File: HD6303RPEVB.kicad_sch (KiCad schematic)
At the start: 36 parts, among them J16 Conn_01x08, J2 Conn_01x06, SW1 Reset, U1 74HC00, U2 HD6303RP, U3 CY62256-70PC, U4 CY62256-70PC, U5 28C64, U6 74HC373, U7 74HC373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

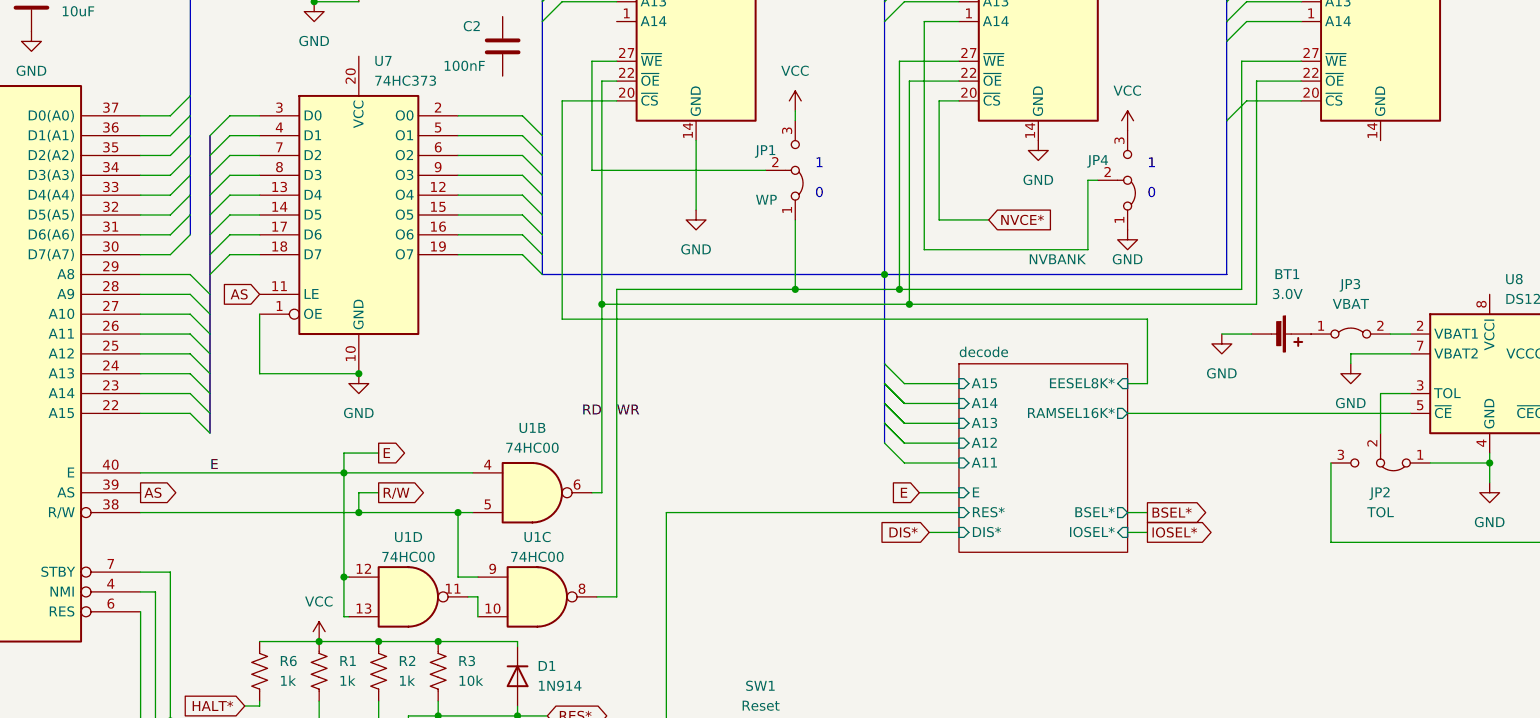
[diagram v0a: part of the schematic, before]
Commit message: Fixed bug in RD/WR circuitry.
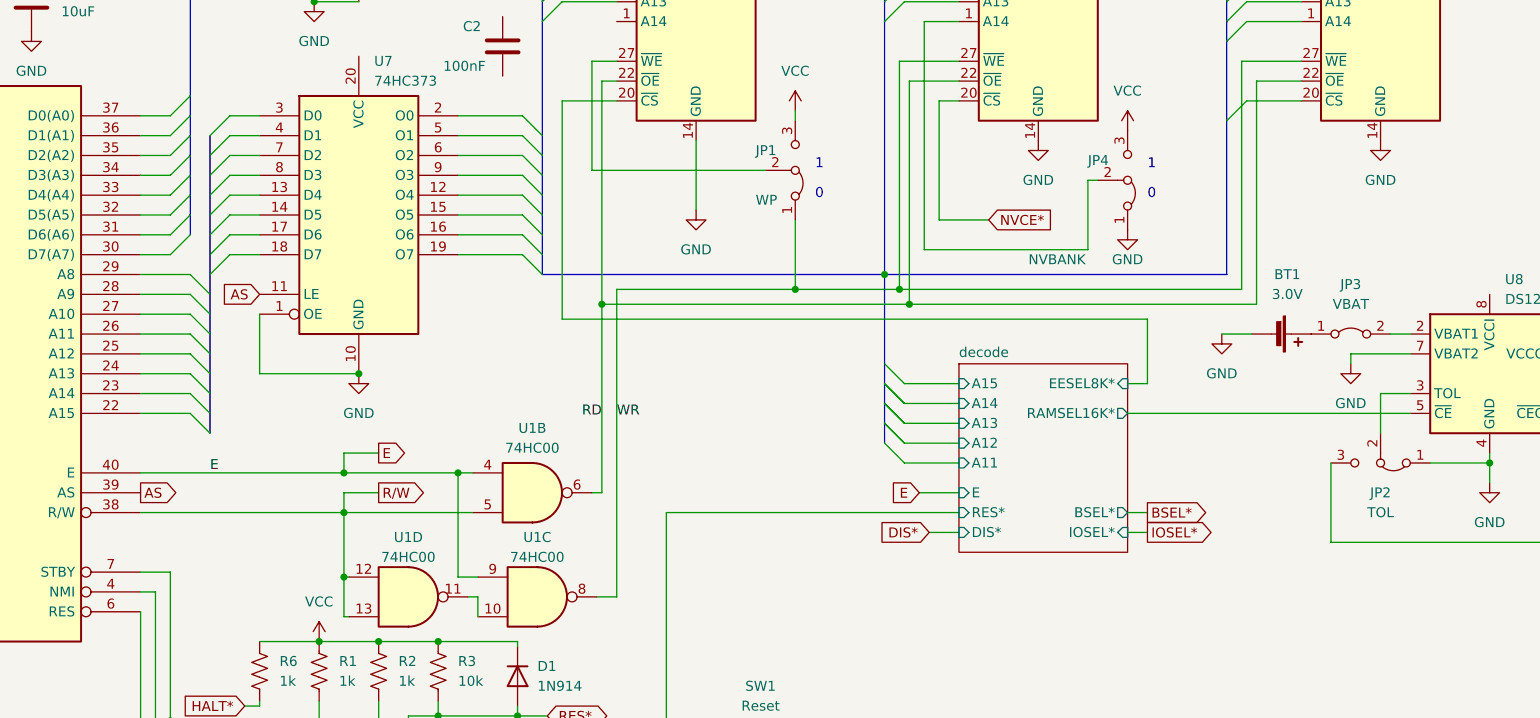
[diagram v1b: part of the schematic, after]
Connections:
- net E: now also U1.9; no longer U1.12, U1.13
- net GND: now also U4.14 (GND)
- net R/W: now also U1.12, U1.13; no longer U1.9
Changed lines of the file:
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@@
 (kicad_sch (version 20230121) (generator eeschema)
   (paper "A4")
-  (junction (at 114.3 165.735) (diameter 0) (color 0 0 0 0)
-  )
   (junction (at 118.745 173.99) (diameter 0) (color 0 0 0 0)
   )
@@
   (junction (at 183.515 127) (diameter 0) (color 0 0 0 0)
   )
-  (junction (at 128.905 157.48) (diameter 0) (color 0 0 0 0)
-  )
   (junction (at 111.125 173.99) (diameter 0) (color 0 0 0 0)
   )
@@
   (junction (at 126.365 173.99) (diameter 0) (color 0 0 0 0)
   )
+  (junction (at 128.905 152.4) (diameter 0) (color 0 0 0 0)
+  )
   (junction (at 90.17 186.055) (diameter 0) (color 0 0 0 0)
   )
@@
   (junction (at 260.985 151.13) (diameter 0) (color 0 0 0 0)
   )
+  (junction (at 114.3 157.48) (diameter 0) (color 0 0 0 0)
+  )
   (junction (at 94.615 43.815) (diameter 0) (color 0 0 0 0)
   )
-  (junction (at 116.205 157.48) (diameter 0) (color 0 0 0 0)
+  (junction (at 114.3 165.735) (diameter 0) (color 0 0 0 0)
   )
   (junction (at 116.205 50.165) (diameter 0) (color 0 0 0 0)
@@
     (stroke (width 0) (type default))
   )
-  (wire (pts (xy 128.905 165.735) (xy 128.905 157.48))
-    (stroke (width 0) (type default))
-  )
   (wire (pts (xy 97.155 71.755) (xy 103.505 71.755))
     (stroke (width 0) (type default))
@@
     (stroke (width 0) (type default))
   )
+  (wire (pts (xy 128.905 152.4) (xy 128.905 165.735))
+    (stroke (width 0) (type default))
+  )
   (wire (pts (xy 131.445 165.735) (xy 128.905 165.735))
     (stroke (width 0) (type default))
@@
     (stroke (width 0) (type default))
   )
-  (wire (pts (xy 116.205 154.94) (xy 116.205 157.48))
+  (wire (pts (xy 114.3 154.94) (xy 114.3 157.48))
     (stroke (width 0) (type default))
   )
@@
     (stroke (width 0) (type default))
   )
-  (wire (pts (xy 114.3 152.4) (xy 114.3 165.735))
-    (stroke (width 0) (type default))
-  )
   (bus (pts (xy 139.7 127) (xy 183.515 127))
     (stroke (width 0) (type default))
@@
     (stroke (width 0) (type default))
   )
-  (wire (pts (xy 128.905 157.48) (xy 130.81 157.48))
+  (wire (pts (xy 114.3 157.48) (xy 130.81 157.48))
     (stroke (width 0) (type default))
   )
@@
     (stroke (width 0) (type default))
   )
-  (wire (pts (xy 118.745 154.94) (xy 116.205 154.94))
+  (wire (pts (xy 118.745 154.94) (xy 114.3 154.94))
     (stroke (width 0) (type default))
   )
@@
     (stroke (width 0) (type default))
   )
+  (wire (pts (xy 128.905 152.4) (xy 130.81 152.4))
+    (stroke (width 0) (type default))
+  )
   (bus (pts (xy 183.515 148.59) (xy 183.515 146.05))
     (stroke (width 0) (type default))
@@
     (stroke (width 0) (type default))
   )
-  (wire (pts (xy 88.265 157.48) (xy 116.205 157.48))
+  (wire (pts (xy 88.265 157.48) (xy 114.3 157.48))
     (stroke (width 0) (type default))
   )
@@
     (stroke (width 0) (type default))
   )
+  (wire (pts (xy 114.3 157.48) (xy 114.3 165.735))
+    (stroke (width 0) (type default))
+  )
   (bus (pts (xy 17.145 60.325) (xy 17.145 62.865))
     (stroke (width 0) (type default))
@@
     (stroke (width 0) (type default))
   )
-  (wire (pts (xy 114.3 152.4) (xy 130.81 152.4))
+  (wire (pts (xy 114.3 152.4) (xy 128.905 152.4))
     (stroke (width 0) (type default))
   )
@@
     (stroke (width 0) (type default))
   )
-  (wire (pts (xy 116.205 157.48) (xy 128.905 157.48))
-    (stroke (width 0) (type default))
-  )
   (wire (pts (xy 37.465 167.64) (xy 17.145 167.64))
     (stroke (width 0) (type default))
@@
         )
       )
+    )
+  )
+  (symbol (lib_id "power:GND") (at 247.015 109.855 0) (unit 1)
+    (in_bom yes) (on_board yes) (dnp no) (fields_autoplaced)
+    (property "Reference" "#PWR011" (at 247.015 116.205 0)
+      (effects (font (size 1.27 1.27)) hide)
+    )
+    (property "Value" "GND" (at 247.015 114.935 0)
+      (effects (font (size 1.27 1.27)))
+    )
+    (property "Footprint" "" (at 247.015 109.855 0)
+      (effects (font (size 1.27 1.27)) hide)
+    )
+    (property "Datasheet" "" (at 247.015 109.855 0)
+      (effects (font (size 1.27 1.27)) hide)
+    )
+    (pin "1")
+    (instances
+      (project "motorino-6303-minimal-plus"
+        (path "/3e8d381f-0d29-4cd1-adc6-483261ac8509"
+          (reference "#PWR011") (unit 1)
+        )
+      )
+      (project "HD6303RPEVB"
+        (path "/41e94b19-4bd8-4c72-aae4-d340f1e5f97f"
+          (reference "#PWR047") (unit 1)
+        )
+      )

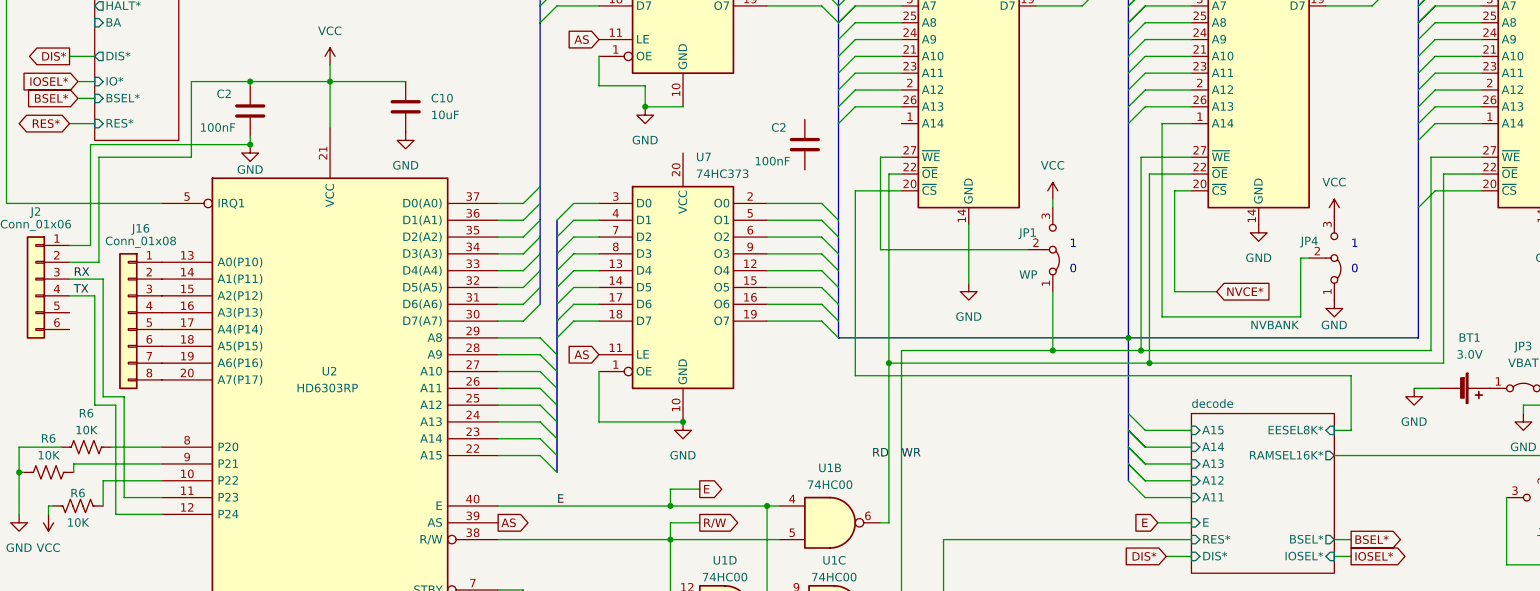
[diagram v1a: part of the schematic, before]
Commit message: NAND, LATCH and NVRAM issues fixed.
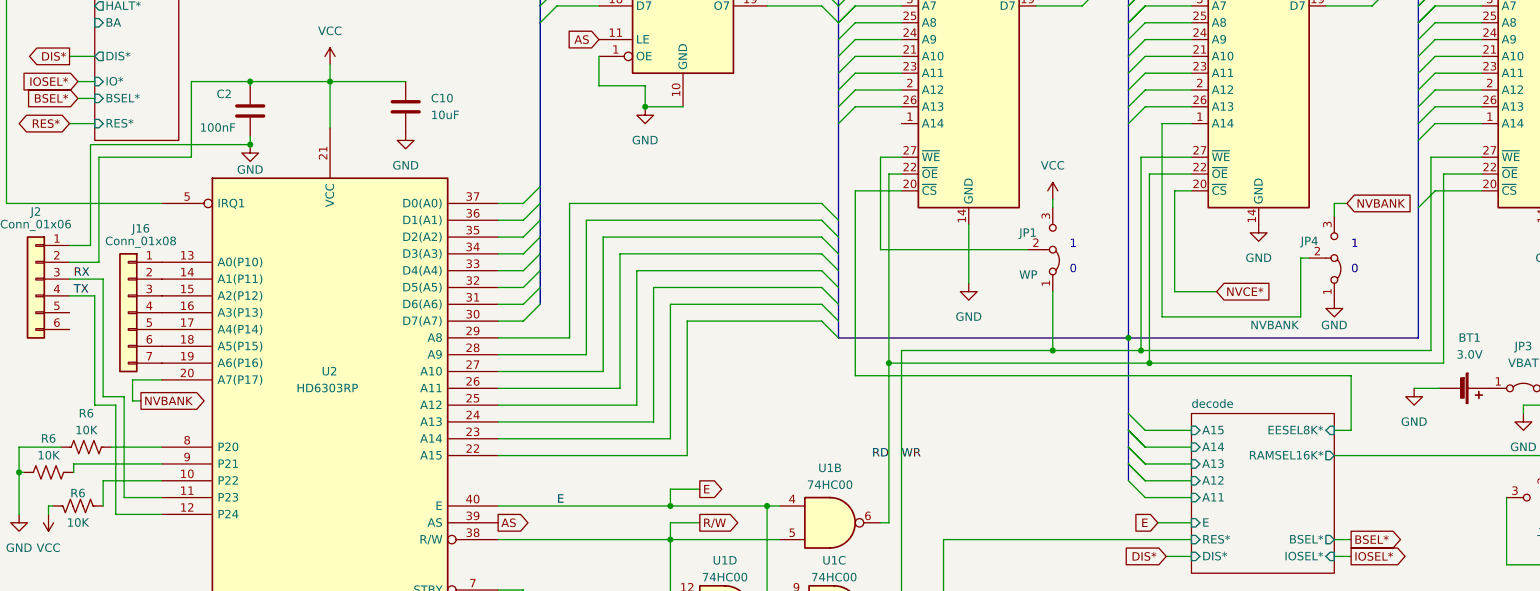
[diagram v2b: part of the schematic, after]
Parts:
- removed C2: 100nF, Capacitor_THT:C_Disc_D8.0mm_W5.0mm_P5.00mm, symbol Device:C
- removed U7: 74HC373, symbol 74xx:74HC373
- J16: symbol Connector_Generic:Conn_01x08 -> Connector_Generic:Conn_01x07
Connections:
- net VCC: no longer JP4.3 (B)
- net NVBANK: now reaches U2.20 (A7(P17))
- net NVBANK: now also JP4.3 (B); no longer J16.8 (Pin_8)

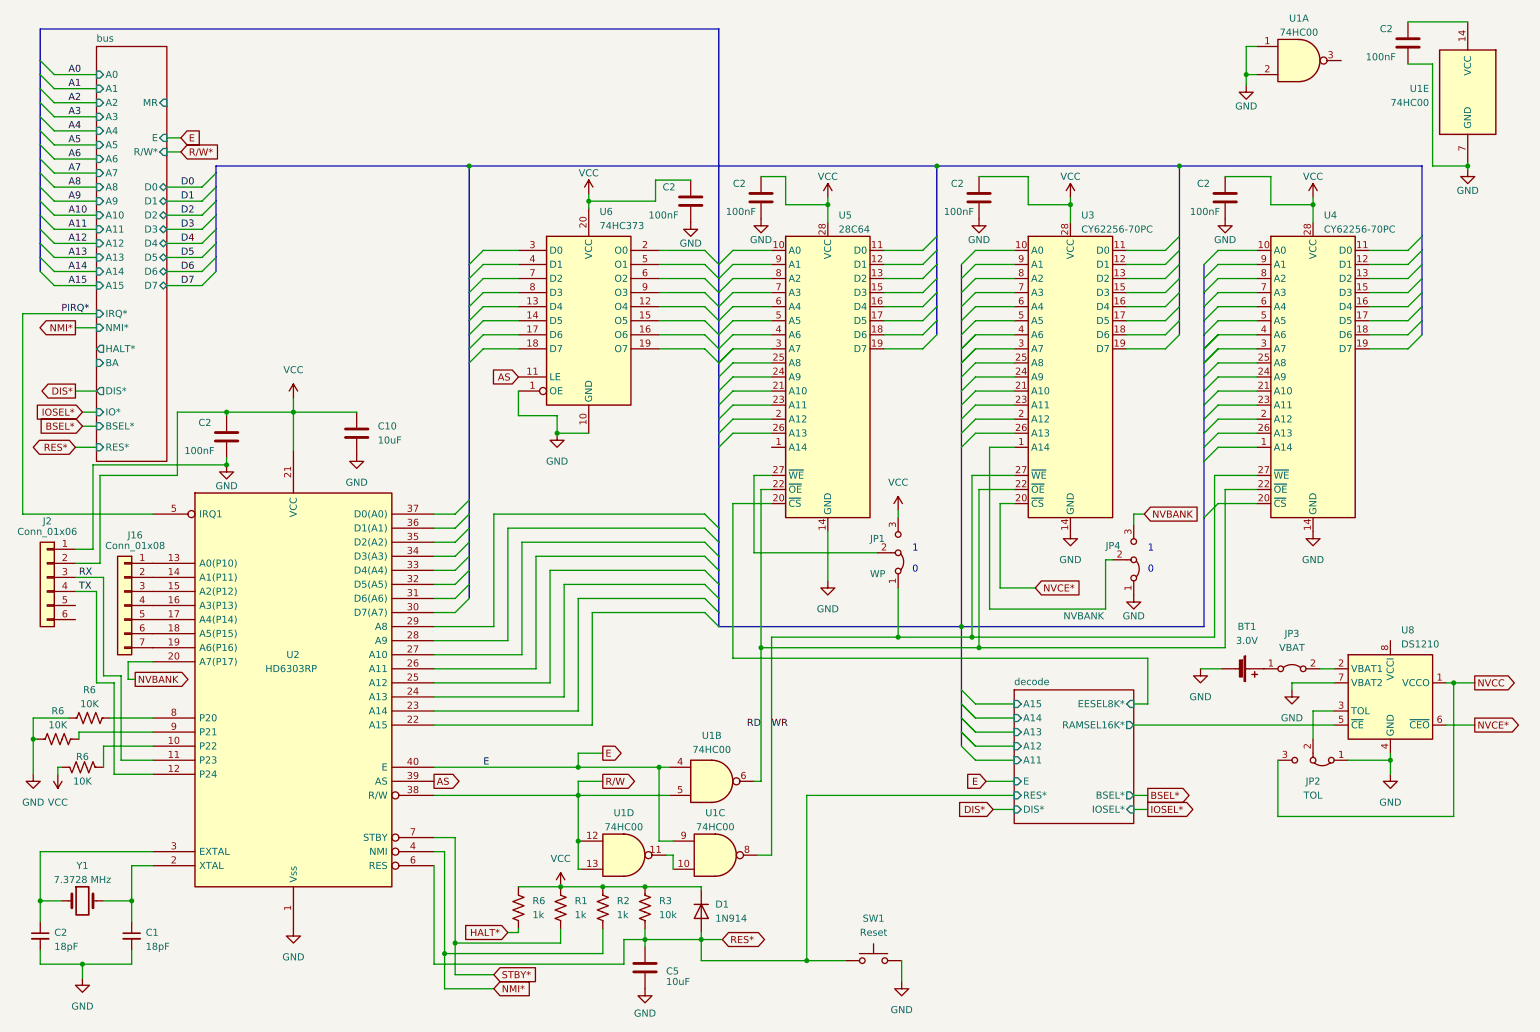
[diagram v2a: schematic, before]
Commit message: Schematic updates
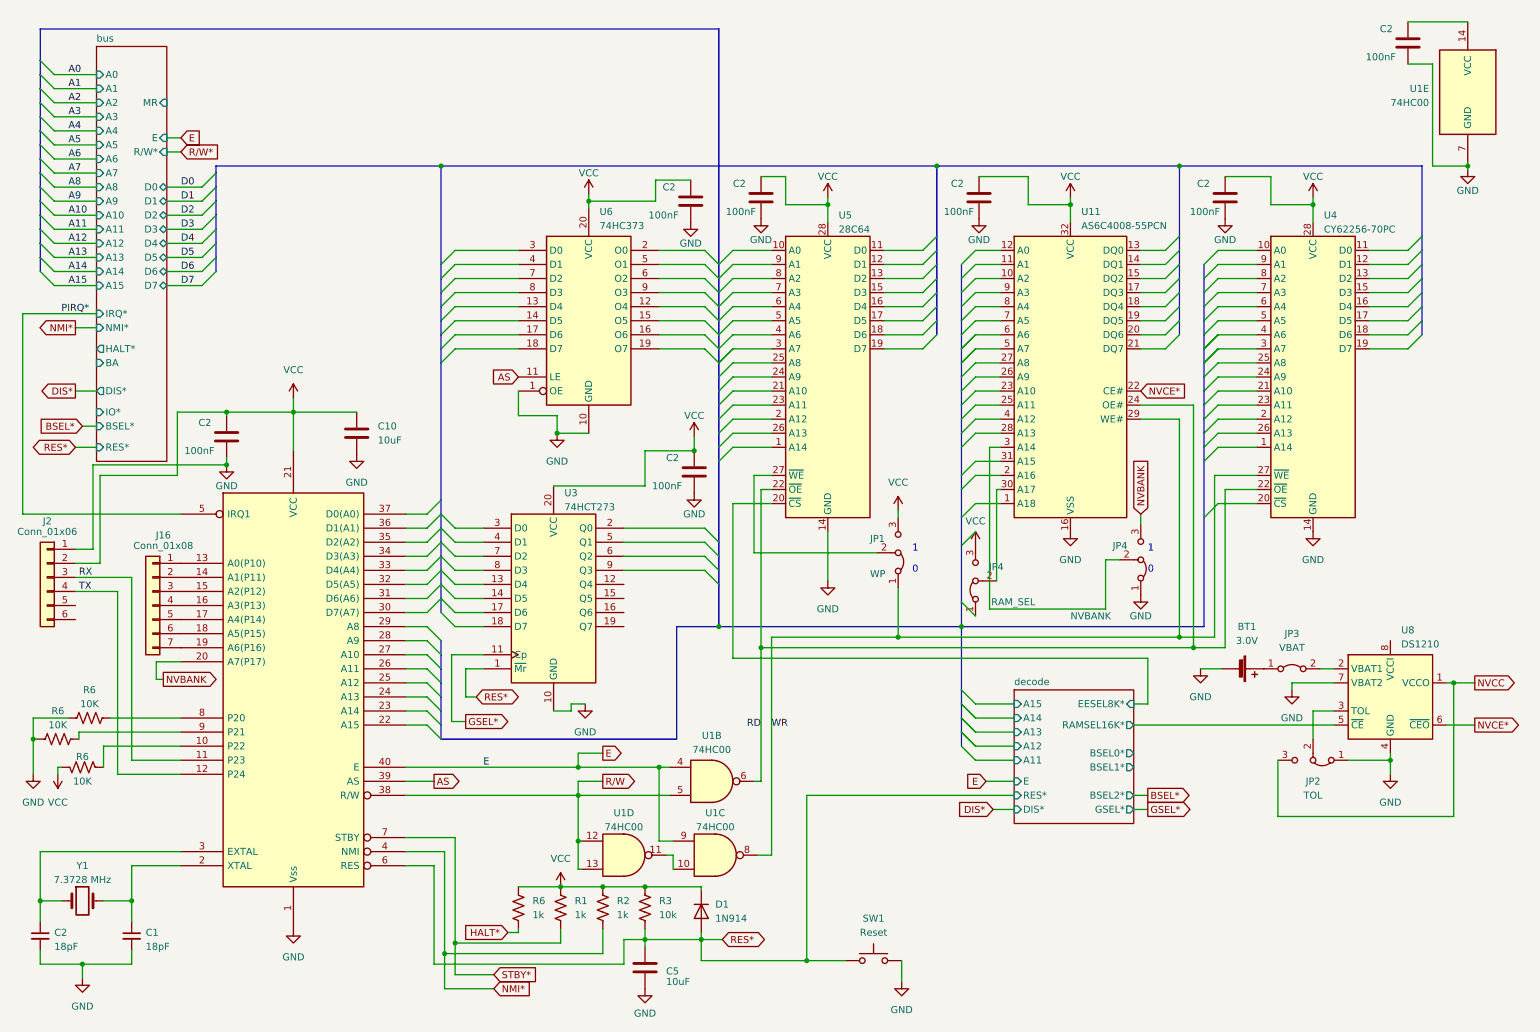
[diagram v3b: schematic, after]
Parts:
- removed unit 1 of U1
- removed U3: CY62256-70PC, symbol Memory_EEPROM:28C256
- added C2: 100nF, Capacitor_THT:C_Disc_D8.0mm_W5.0mm_P5.00mm, symbol Device:C
- added JP4: RAM_SEL, Connector_PinHeader_2.54mm:PinHeader_1x03_P2.54mm_Vertical, symbol Jumper:Jumper_3_Bridged12
- added U11: AS6C4008-55PCN, Package_DIP:DIP-32_W15.24mm, symbol Memory_RAM:AS6C4008-55PCN
- added U3: 74HCT273, symbol 74xx:74HCT273
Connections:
- net GND: now also C2.2, U11.16 (VSS), U3.10 (GND)
- net NVCE*: now also U11.22 (CE#)
- net RD: now also U11.24 (OE#)
- net RES*: now also U3.1 (~{Mr})
- net VCC: now also C2.1, JP4.3 (B), U11.32 (VCC), U3.20 (VCC)
- net WR: now also U11.29 (WE#)
- net at JP4.2 (C): now also U11.3 (A14)
- new net: JP4.2 (C), U11.30 (A17)
- new net GSEL*: U3.11 (Cp)
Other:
- sheet decode ports: added BSEL0*, BSEL1*, BSEL2*, GSEL*; removed BSEL*, IOSEL*
- moved on the sheet: J16, JP4
